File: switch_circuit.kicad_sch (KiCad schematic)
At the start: 5 parts, among them J5 USB_OUT, Q2 Q_NMOS_GDS, U3 INA219AxD

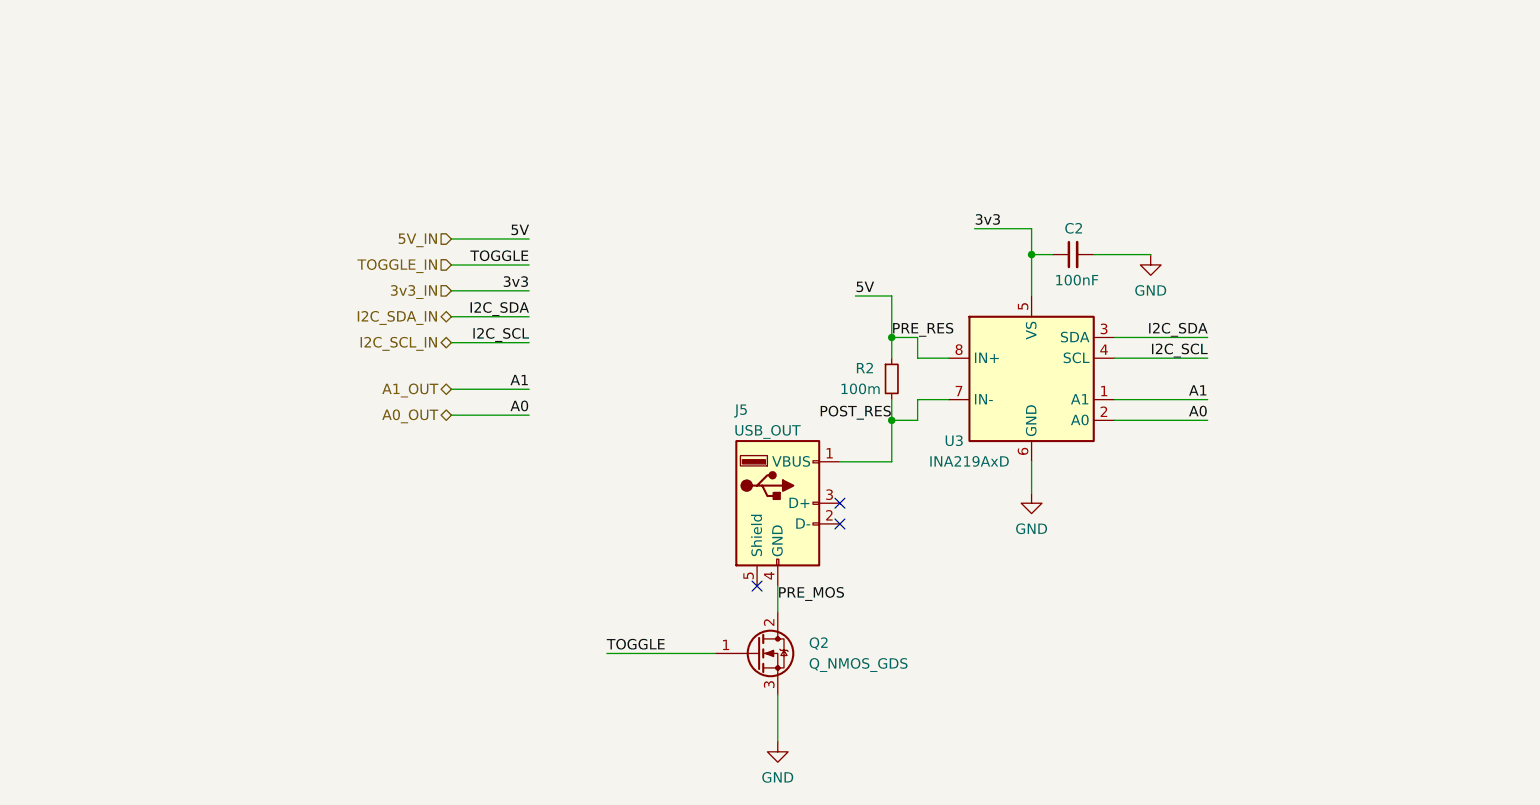
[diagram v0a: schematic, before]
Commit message: Made schematics pretty, added photos, added README
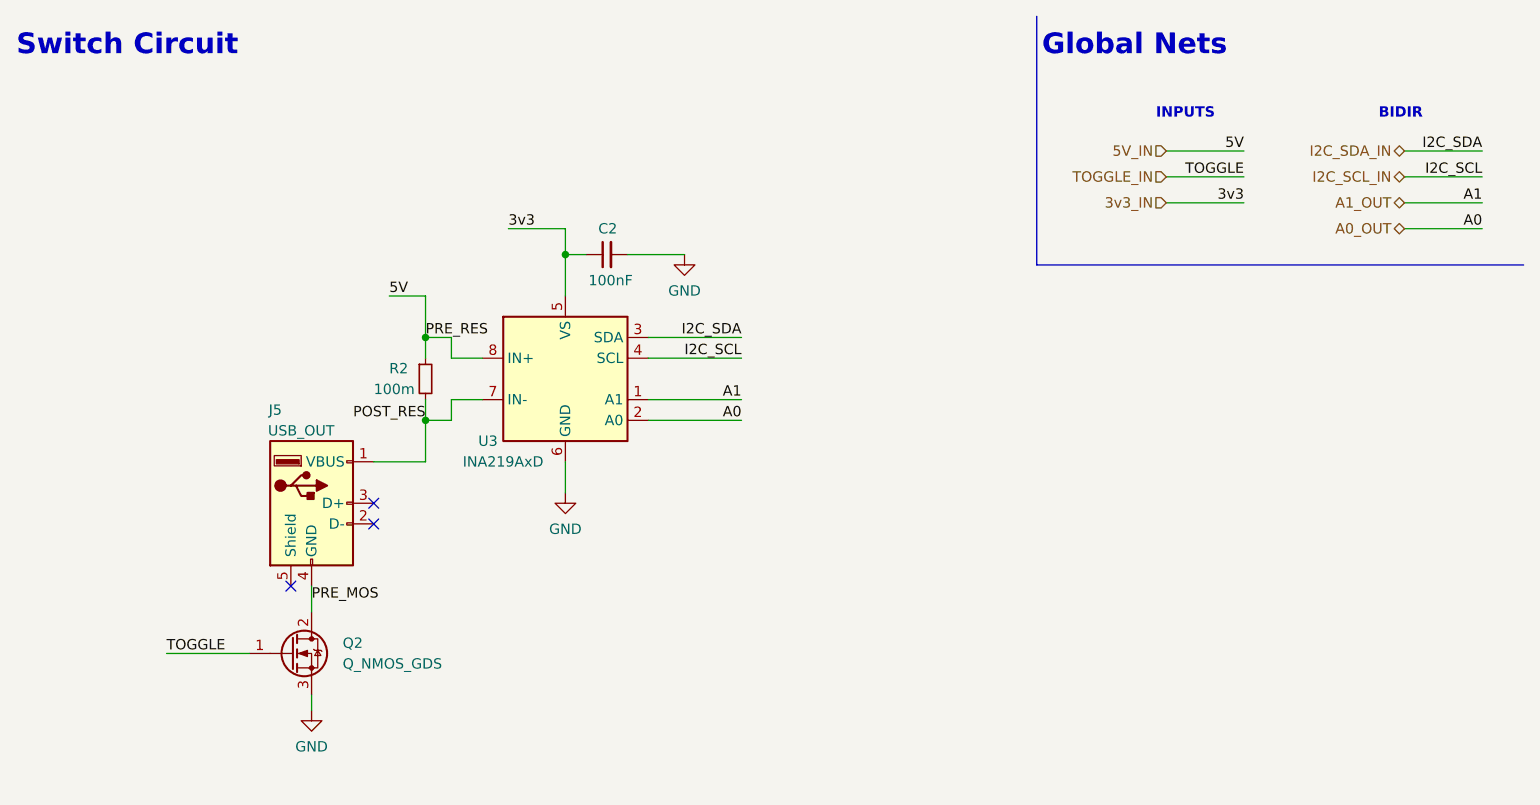
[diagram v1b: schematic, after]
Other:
- note added: "BIDIR"
- note added: "Global Nets"
- note added: "INPUTS"
- note added: "Switch Circuit"
- title: (none) -> Wifi USB Port
- moved on the sheet: C2, J5, Q2, R2, U3
